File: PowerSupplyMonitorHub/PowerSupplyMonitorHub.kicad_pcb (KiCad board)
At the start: 2 copper layers, 88 parts, among them J1 Input, J10 RJ45 PWR 4, J2 OLED I2C, J3 CON_PCA, J4 RJ45 PWR 0, J5 CON_PCF, J6 RJ45 PWR 1, J7 RJ45 PWR 2, J8 CON_TCA, J9 RJ45 PWR 3, SW1 DIP_PCA, SW2 DIP_PCF, SW3 DIP_TCA, U1 PCA9685PW, U10 PC817, U11 PC817, U12 PC817, U13 PC817, U3 PC817, U4 PC817, U5 PC817, U6 PC817, U7 PC817, U8 PC817, U9 TCA9548APWR

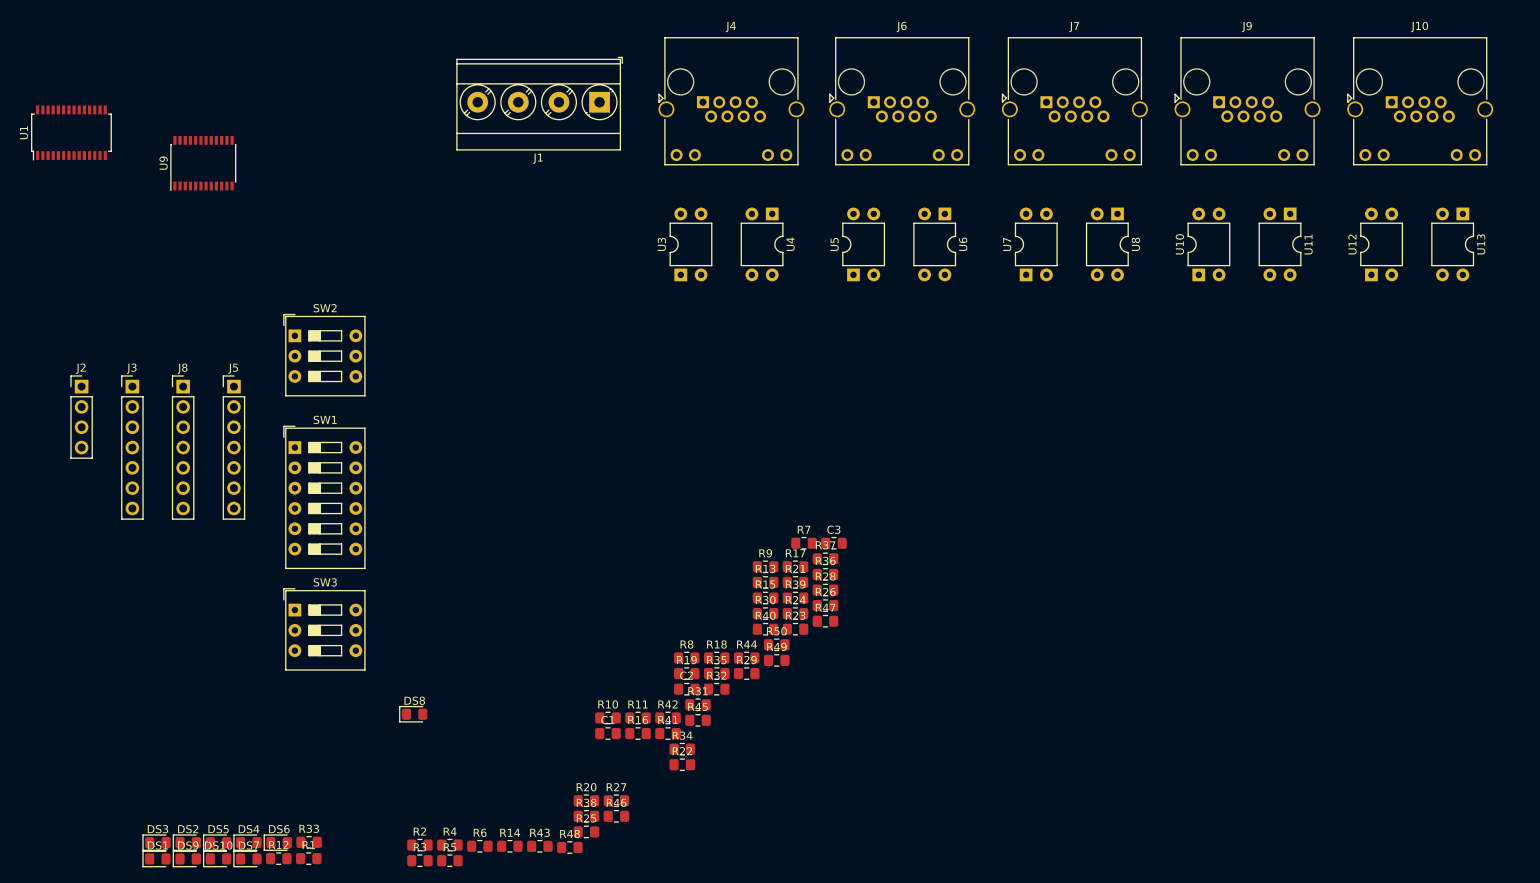
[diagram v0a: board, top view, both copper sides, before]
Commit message: added dip switches to i2c ics for adress selection added pullup resistors to i2c input lines added placeholder footprint for pcf8575 added minimal pcb placement for testing
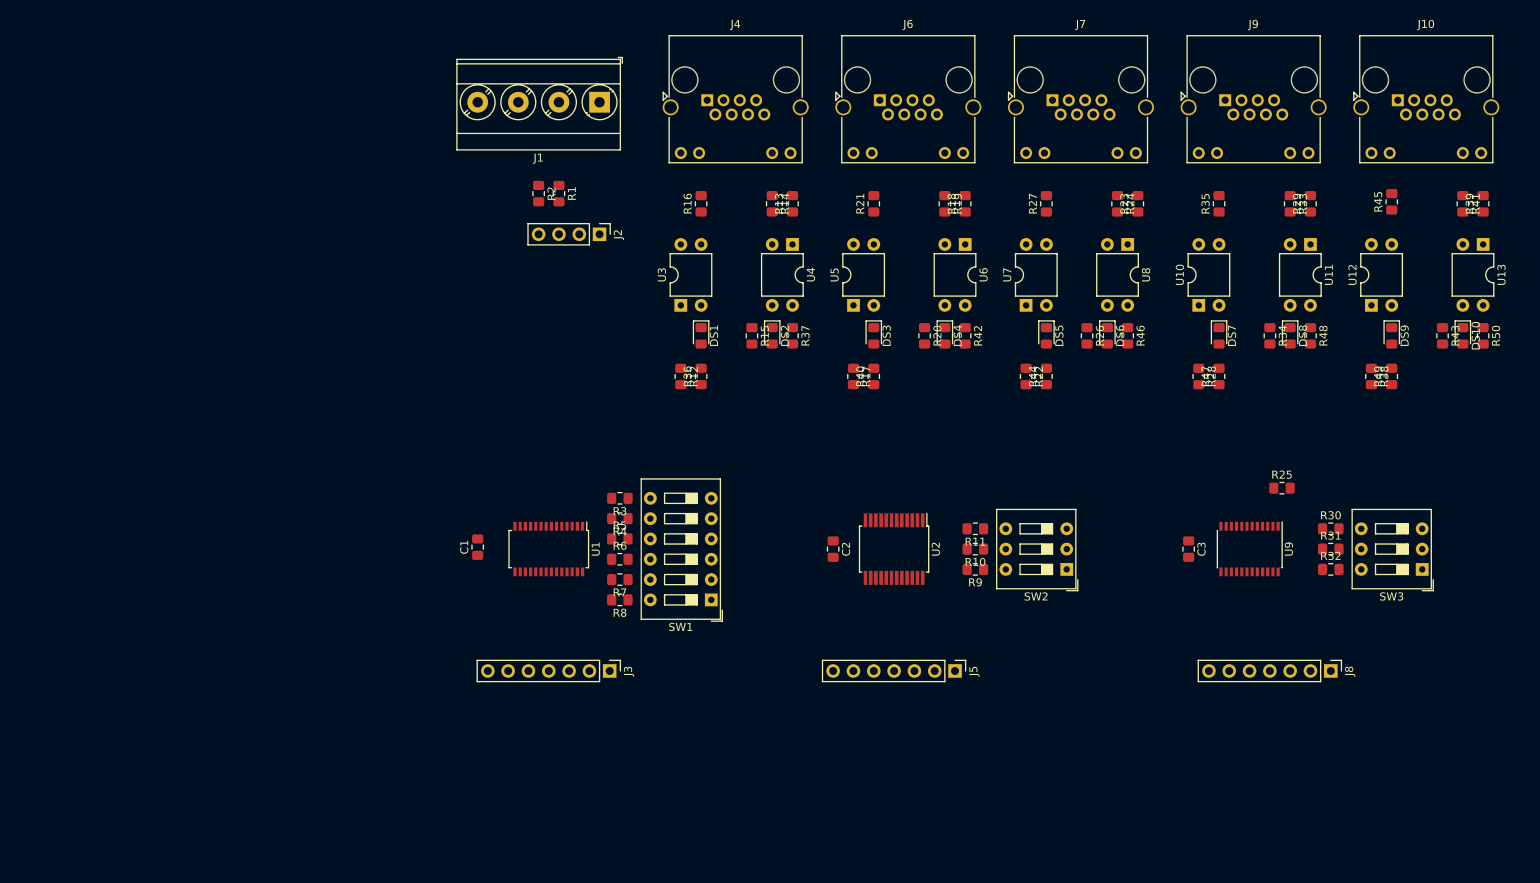
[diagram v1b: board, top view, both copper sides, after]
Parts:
- added U2: PCF8575, Package_SO:SSOP-24_5.3x8.2mm_P0.65mm, F.Cu at (148.6, 94.0)
- DS1: value DC0 -> RC0
- DS10: value RC4 -> DC4
- DS2: value RC0 -> DC0
- DS3: value DC1 -> RC1
- DS4: value RC1 -> DC1
- DS5: value DC2 -> RC2
- DS6: value RC2 -> DC2
- DS7: value DC3 -> RC3
- DS8: value RC3 -> DC3
- DS9: value DC4 -> RC4
- moved DS10 168.8 mm to (219.7, 67.3), turned to 270 degrees
- moved DS9 164.1 mm to (210.8, 67.3), turned to 270 degrees
- moved J8 147.9 mm to (203.2, 109.2), turned to 270 degrees
- moved R33 146.4 mm to (198.1, 50.8), turned to 270 degrees
- moved SW3 141.1 mm to (214.6, 96.5), turned to 180 degrees
- moved U9 139.4 mm to (193.0, 94.0), turned to 270 degrees
- moved DS7 137.8 mm to (189.2, 67.3), turned to 270 degrees
- moved R43 129.7 mm to (217.2, 67.3), turned to 270 degrees
- moved DS6 121.4 mm to (175.3, 67.3), turned to 270 degrees
- moved DS5 121.4 mm to (167.6, 67.3), turned to 270 degrees
- moved R41 119.4 mm to (219.7, 50.8), turned to 270 degrees
- moved DS8 119.3 mm to (198.1, 67.3), turned to 270 degrees
- moved R48 112.6 mm to (200.7, 67.3), turned to 270 degrees
- moved R38 112.5 mm to (208.3, 72.4), turned to 270 degrees
- moved DS3 109.7 mm to (146.1, 67.3), turned to 270 degrees
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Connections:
- DS1 pad 1: /DC_0 -> /RC_0
- DS10 pad 1: /RC_4 -> /DC_4
- DS2 pad 1: /RC_0 -> /DC_0
- DS3 pad 1: /DC_1 -> /RC_1
- DS4 pad 1: /RC_1 -> /DC_1
- DS5 pad 1: /DC_2 -> /RC_2
- DS6 pad 1: /RC_2 -> /DC_2
- DS7 pad 1: /DC_3 -> /RC_3
- DS8 pad 1: /RC_3 -> /DC_3
- DS9 pad 1: /DC_4 -> /RC_4

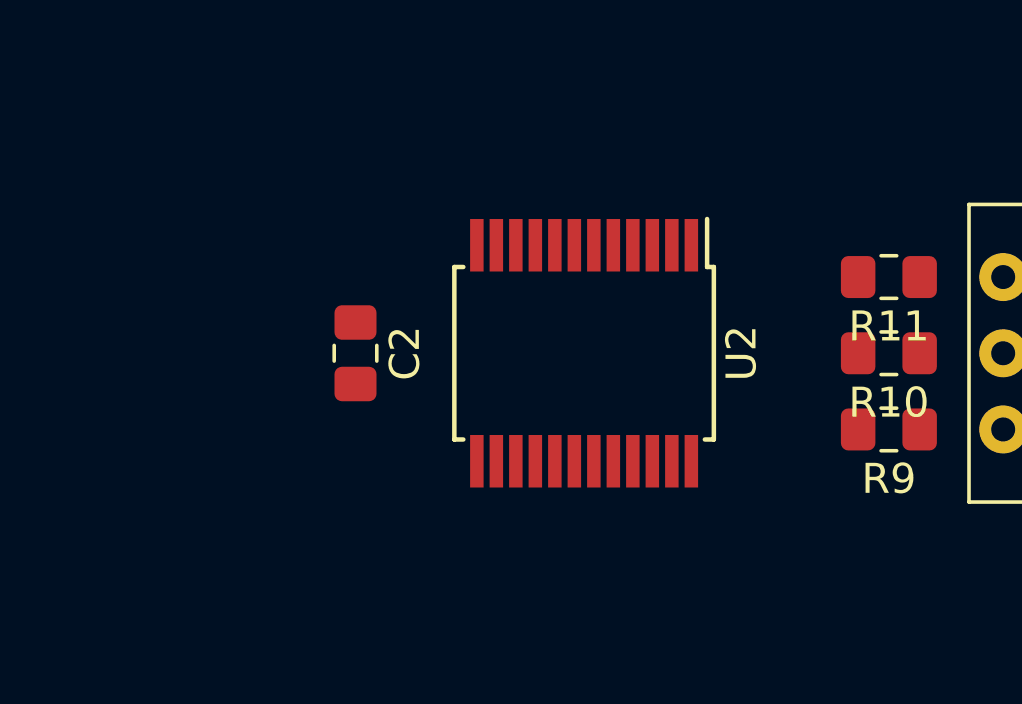
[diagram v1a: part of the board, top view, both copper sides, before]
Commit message: changed package and footprint from sop to soi for pcf8575
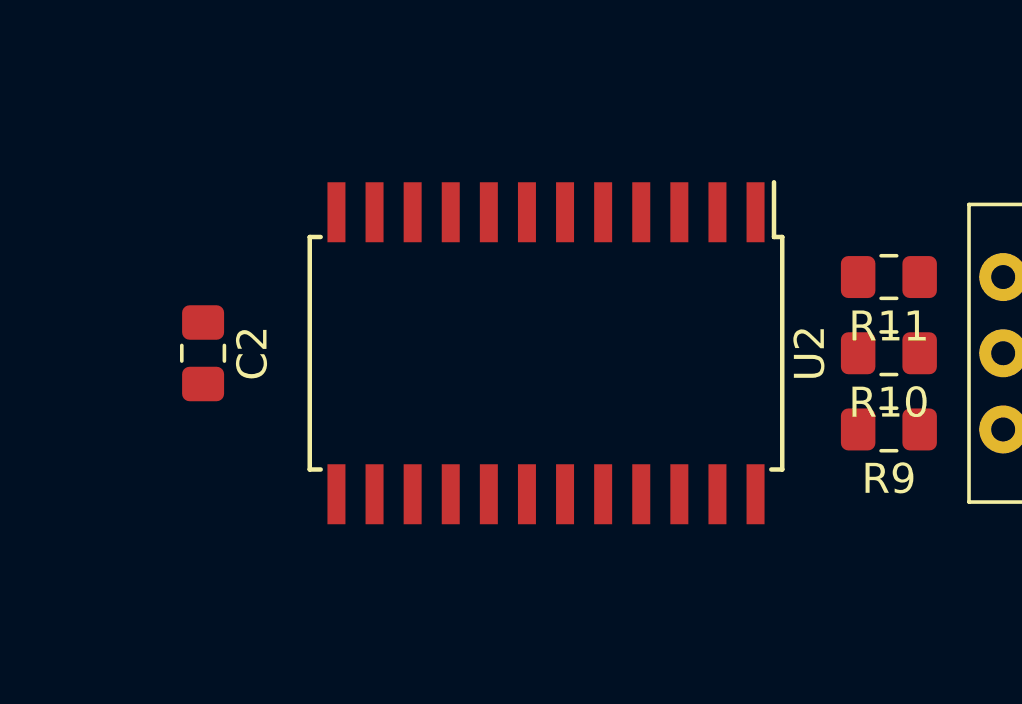
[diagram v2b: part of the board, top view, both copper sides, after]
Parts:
- U2: footprint Package_SO:SSOP-24_5.3x8.2mm_P0.65mm -> Package_SO:SOIC-24W_7.5x15.4mm_P1.27mm
- moved C2 5.08 mm to (135.9, 94.0)
- moved U2 1.27 mm to (147.3, 94.0)

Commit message: added new 3d render of front and back view of pcb added pcb routing from autorouter added power led indicator added i2c ic adress ranges to silkscreen added unused ic pins pinout info silkscreen added power input info silkscreen
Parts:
- added DS11: PWR, LED_SMD:LED_0805_2012Metric_Pad1.15x1.40mm_HandSolder, F.Cu at (104.8, 94.6)
- added G***: LOGO, w_logo:Logo_silk_OSHW_6x6mm, F.Cu at (87.6, 112.4)
- added G***: LOGO, w_logo:Logo_copper_OSHW_6x6mm, B.Cu at (87.6, 112.4)
- added MH1: MountingHole, MountingHole:MountingHole_3.5mm, F.Cu at (86.3, 70.2)
- added MH2: MountingHole, MountingHole:MountingHole_3.5mm, F.Cu at (223.3, 70.2)
- added MH3: MountingHole, MountingHole:MountingHole_3.5mm, F.Cu at (223.3, 124.2)
- added MH4: MountingHole, MountingHole:MountingHole_3.5mm, F.Cu at (86.3, 124.2)
- added R51: 220, Resistor_SMD:R_0805_2012Metric_Pad1.15x1.40mm_HandSolder, F.Cu at (102.2, 94.6)
- J1: value Input -> PCA; footprint TerminalBlock_Phoenix:TerminalBlock_Phoenix_MKDS-3-4-5.08_1x04_P5.08mm_Horizontal -> Connector_PinHeader_2.54mm:PinHeader_1x07_P2.54mm_Vertical
- J10: value RJ45 PWR 4 -> Input; footprint Connector_RJ:RJ45_Amphenol_RJHSE538X -> TerminalBlock_Phoenix:TerminalBlock_Phoenix_MKDS-3-4-5.08_1x04_P5.08mm_Horizontal
- J2: value OLED I2C -> RJ45 PWR 0; footprint Connector_PinHeader_2.54mm:PinHeader_1x04_P2.54mm_Vertical -> Connector_RJ:RJ45_Amphenol_RJHSE538X
- J3: value CON_PCA -> RJ45 PWR 1; footprint Connector_PinHeader_2.54mm:PinHeader_1x07_P2.54mm_Vertical -> Connector_RJ:RJ45_Amphenol_RJHSE538X
- J4: value RJ45 PWR 0 -> RJ45 PWR 2
- J5: value CON_PCF -> RJ45 PWR 3; footprint Connector_PinHeader_2.54mm:PinHeader_1x07_P2.54mm_Vertical -> Connector_RJ:RJ45_Amphenol_RJHSE538X
- J6: value RJ45 PWR 1 -> RJ45 PWR 4
- J7: value RJ45 PWR 2 -> OLED I2C; footprint Connector_RJ:RJ45_Amphenol_RJHSE538X -> Connector_PinHeader_2.54mm:PinHeader_1x04_P2.54mm_Vertical
- J8: value CON_TCA -> TCA
- J9: value RJ45 PWR 3 -> PCF; footprint Connector_RJ:RJ45_Amphenol_RJHSE538X -> Connector_PinHeader_2.54mm:PinHeader_1x07_P2.54mm_Vertical
- R1, R10, R11, R2, R25, R3, R30, R4, R5, R6, R7, R8, R9: value 10K -> 220
- R16, R17, R18, R19, R20, R33, R34, R35, R36, R37, R48, R49, R50: value 220 -> 10K
- SW2: value DIP_PCF -> DIP_TCA
- SW3: value DIP_TCA -> DIP_PCF
- U12: value PC817 -> TCA9548APWR; footprint Package_DIP:DIP-4_W7.62mm -> Package_SO:TSSOP-24_4.4x7.8mm_P0.65mm
- U13: value PC817 -> PCF8575; footprint Package_DIP:DIP-4_W7.62mm -> Package_SO:SOIC-24W_7.5x15.4mm_P1.27mm
- U2: value PCF8575 -> PC817; footprint Package_SO:SOIC-24W_7.5x15.4mm_P1.27mm -> Package_DIP:DIP-4_W7.62mm
- U9: value TCA9548APWR -> PC817; footprint Package_SO:TSSOP-24_4.4x7.8mm_P0.65mm -> Package_DIP:DIP-4_W7.62mm
- moved R33 110.0 mm to (97.2, 94.6), turned to 90 degrees
- moved J10 108.8 mm to (108.6, 73.0), turned to 180 degrees
- moved R39 107.5 mm to (128.9, 104.1), turned to 180 degrees
- moved R32 103.5 mm to (99.7, 94.6), turned to 90 degrees
- moved R36 97.9 mm to (208.9, 121.9)
- moved R38 96.2 mm to (117.5, 104.1), turned to 0 degrees
- moved R37 93.2 mm to (211.5, 121.9), turned to 90 degrees
- moved U13 92.5 mm to (150.5, 114.3)
- moved J9 92.3 mm to (158.1, 124.5), turned to 270 degrees
- moved R41 87.4 mm to (150.5, 104.1), turned to 180 degrees
- moved R15 86.6 mm to (215.3, 86.4), turned to 0 degrees
- moved J1 86.4 mm to (108.6, 124.5), turned to 270 degrees
- moved J7 82.0 mm to (104.8, 89.5), turned to 270 degrees
- moved R31 81.8 mm to (126.4, 121.9), turned to 270 degrees
- moved R18 81.0 mm to (118.7, 121.9), turned to 270 degrees
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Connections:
- DS10 pad 1: /DC_4 -> GND
- DS2 pad 1: /DC_0 -> GND
- DS4 pad 1: /DC_1 -> GND
- DS6 pad 1: /DC_2 -> GND
- DS8 pad 1: /DC_3 -> GND
- J1 pad 2: +5V -> Net-(J1-Pad2)
- J1 pad 3: /SCL -> Net-(J1-Pad3)
- J1 pad 4: /SDA -> Net-(J1-Pad4)
- J10 pad 1: /RC+_4 -> GND
- J10 pad 2: /RC-_4 -> +5V
- J10 pad 3: /DC-OK_4 -> /SCL
- J10 pad 4: /SCL4 -> /SDA
- J2 pad 1: GND -> /RC+_0
- J2 pad 2: +5V -> /RC-_0
- J2 pad 3: /SCL -> /DC-OK_0
- J2 pad 4: /SDA -> /SCL0
- J3 pad 1: GND -> /RC+_1
- J3 pad 2: Net-(J3-Pad2) -> /RC-_1
- J3 pad 3: Net-(J3-Pad3) -> /DC-OK_1
- J3 pad 4: Net-(J3-Pad4) -> /SCL1
- J3 pad 5: Net-(J3-Pad5) -> GND
- J3 pad 6: Net-(J3-Pad6) -> /DC-GND_1
- J3 pad 7: Net-(J3-Pad7) -> /SDA1
- J4 pad 1: /RC+_0 -> /RC+_2
- J4 pad 2: /RC-_0 -> /RC-_2
- J4 pad 3: /DC-OK_0 -> /DC-OK_2
- J4 pad 4: /SCL0 -> /SCL2
- J4 pad 6: /DC-GND_0 -> /DC-GND_2
- J4 pad 7: /SDA0 -> /SDA2
- J5 pad 1: +5V -> /RC+_3
- J5 pad 2: Net-(J5-Pad2) -> /RC-_3
- J5 pad 3: Net-(J5-Pad3) -> /DC-OK_3
- J5 pad 4: Net-(J5-Pad4) -> /SCL3
- J5 pad 5: Net-(J5-Pad5) -> GND
- J5 pad 6: Net-(J5-Pad6) -> /DC-GND_3
- J5 pad 7: Net-(J5-Pad7) -> /SDA3
- J6 pad 1: /RC+_1 -> /RC+_4
- J6 pad 2: /RC-_1 -> /RC-_4
- J6 pad 3: /DC-OK_1 -> /DC-OK_4
- J6 pad 4: /SCL1 -> /SCL4
- J6 pad 6: /DC-GND_1 -> /DC-GND_4
- J6 pad 7: /SDA1 -> /SDA4
- J7 pad 1: /RC+_2 -> GND
- J7 pad 2: /RC-_2 -> +5V
- J7 pad 3: /DC-OK_2 -> /SCL
- J7 pad 4: /SCL2 -> /SDA
- J9 pad 1: /RC+_3 -> +5V
- J9 pad 2: /RC-_3 -> Net-(J9-Pad2)
- J9 pad 3: /DC-OK_3 -> Net-(J9-Pad3)
- J9 pad 4: /SCL3 -> Net-(J9-Pad4)
- J9 pad 5: GND -> Net-(J9-Pad5)
- J9 pad 6: /DC-GND_3 -> Net-(J9-Pad6)
- J9 pad 7: /SDA3 -> Net-(J9-Pad7)
- R1 pad 1: +5V -> /DATA_0
- R1 pad 2: /SCL -> Net-(J2-Pad12)
- R10 pad 1: Net-(R10-Pad1) -> /LINK_4
- R10 pad 2: GND -> Net-(J6-Pad10)
- R11 pad 1: Net-(R11-Pad1) -> /DC-OK_0
- R11 pad 2: GND -> Net-(R11-Pad2)
- R12 pad 1: Net-(R12-Pad1) -> /DC-OK_1
- R12 pad 2: +5V -> Net-(R12-Pad2)
- R13 pad 1: /DATA_0 -> /DC-OK_2
- R13 pad 2: Net-(J4-Pad12) -> Net-(R13-Pad2)
- R14 pad 1: /DC-OK_0 -> /DC-OK_3
- R15 pad 1: /DC_0 -> /DC-OK_4
- R15 pad 2: GND -> Net-(R15-Pad2)
- R16 pad 1: /LINK_0 -> Net-(R16-Pad1)
- R16 pad 2: Net-(J4-Pad10) -> GND
- R17 pad 2: +5V -> GND
- R18 pad 1: /DATA_1 -> Net-(R18-Pad1)
- R18 pad 2: Net-(J6-Pad12) -> GND
- R19 pad 1: /DC-OK_1 -> Net-(R19-Pad1)
- R19 pad 2: Net-(R19-Pad2) -> GND
- R2 pad 1: +5V -> /LINK_0
- R2 pad 2: /SDA -> Net-(J2-Pad10)
- R20 pad 1: /DC_1 -> Net-(R20-Pad1)
- R21 pad 1: /LINK_1 -> Net-(R21-Pad1)
- R21 pad 2: Net-(J6-Pad10) -> +5V
- R23 pad 1: /DATA_2 -> Net-(R23-Pad1)
- R23 pad 2: Net-(J7-Pad12) -> +5V
- R24 pad 1: /DC-OK_2 -> Net-(R24-Pad1)
- R24 pad 2: Net-(R24-Pad2) -> +5V
- R26 pad 1: /DC_2 -> Net-(R26-Pad1)
- R26 pad 2: GND -> +5V
- R27 pad 1: /LINK_2 -> Net-(R27-Pad1)
- R27 pad 2: Net-(J7-Pad10) -> +5V
- R29 pad 1: /DATA_3 -> Net-(R29-Pad1)
- R29 pad 2: Net-(J9-Pad12) -> +5V
- R3 pad 1: Net-(R3-Pad1) -> /DATA_1
- R3 pad 2: GND -> Net-(J3-Pad12)
- R30 pad 1: GND -> Net-(R30-Pad1)
- R30 pad 2: Net-(R30-Pad2) -> +5V
- R31 pad 1: GND -> Net-(R31-Pad1)
- R31 pad 2: Net-(R31-Pad2) -> GND
- R32 pad 1: GND -> +5V
- R32 pad 2: Net-(R32-Pad2) -> /SCL
- R33 pad 1: /DC-OK_3 -> +5V
- R33 pad 2: Net-(R33-Pad2) -> /SDA
- R34 pad 1: /DC_3 -> GND
- R34 pad 2: GND -> Net-(R34-Pad2)
- R35 pad 1: /LINK_3 -> Net-(R35-Pad1)
- R35 pad 2: Net-(J9-Pad10) -> +5V
- R36 pad 1: +5V -> GND
- R36 pad 2: Net-(DS1-Pad2) -> Net-(R36-Pad2)
- R37 pad 1: +5V -> GND
- R37 pad 2: Net-(DS2-Pad2) -> Net-(R37-Pad2)
- R38 pad 1: Net-(R38-Pad1) -> +5V
- R38 pad 2: +5V -> Net-(DS1-Pad2)
- R39 pad 1: /DATA_4 -> +5V
- R39 pad 2: Net-(J10-Pad12) -> Net-(DS2-Pad2)
- R4 pad 1: Net-(R4-Pad1) -> /LINK_1
- R4 pad 2: GND -> Net-(J3-Pad10)
- R41 pad 1: /DC-OK_4 -> +5V
- R41 pad 2: Net-(R41-Pad2) -> Net-(DS4-Pad2)
- R42 pad 2: Net-(DS4-Pad2) -> Net-(DS5-Pad2)
- R43 pad 1: /DC_4 -> +5V
- R43 pad 2: GND -> Net-(DS6-Pad2)
- R44 pad 2: Net-(DS5-Pad2) -> Net-(DS7-Pad2)
- R45 pad 1: /LINK_4 -> +5V
- R45 pad 2: Net-(J10-Pad10) -> Net-(DS8-Pad2)
- R46 pad 2: Net-(DS6-Pad2) -> Net-(DS9-Pad2)
- R47 pad 2: Net-(DS7-Pad2) -> Net-(DS10-Pad2)
- R48 pad 1: +5V -> Net-(R48-Pad1)
- R48 pad 2: Net-(DS8-Pad2) -> GND
- R49 pad 1: +5V -> Net-(R49-Pad1)
- R49 pad 2: Net-(DS9-Pad2) -> GND
- R5 pad 1: Net-(R5-Pad1) -> /DATA_2
- R5 pad 2: GND -> Net-(J4-Pad12)
- R50 pad 1: +5V -> Net-(R50-Pad1)
- R50 pad 2: Net-(DS10-Pad2) -> GND
- R6 pad 1: Net-(R6-Pad1) -> /LINK_2
- R6 pad 2: GND -> Net-(J4-Pad10)
- R7 pad 1: Net-(R7-Pad1) -> /DATA_3
- R7 pad 2: GND -> Net-(J5-Pad12)
- R8 pad 1: Net-(R8-Pad1) -> /LINK_3
- R8 pad 2: GND -> Net-(J5-Pad10)
- R9 pad 1: Net-(R9-Pad1) -> /DATA_4
- R9 pad 2: GND -> Net-(J6-Pad12)
- SW1 pad 10: Net-(R6-Pad1) -> Net-(R19-Pad1)
- SW1 pad 11: Net-(R7-Pad1) -> Net-(R20-Pad1)
- SW1 pad 12: Net-(R8-Pad1) -> Net-(R31-Pad1)
- SW1 pad 7: Net-(R3-Pad1) -> Net-(R16-Pad1)
- SW1 pad 8: Net-(R4-Pad1) -> Net-(R17-Pad1)
- SW1 pad 9: Net-(R5-Pad1) -> Net-(R18-Pad1)
- SW2 pad 4: Net-(R11-Pad1) -> Net-(R34-Pad2)
- SW2 pad 5: Net-(R10-Pad1) -> Net-(R36-Pad2)
- SW2 pad 6: Net-(R9-Pad1) -> Net-(R37-Pad2)
- SW3 pad 4: Net-(R30-Pad2) -> Net-(R50-Pad1)
- SW3 pad 5: Net-(R31-Pad2) -> Net-(R49-Pad1)
- SW3 pad 6: Net-(R32-Pad2) -> Net-(R48-Pad1)
- U1 pad 1: Net-(R8-Pad1) -> Net-(R31-Pad1)
- U1 pad 17: Net-(J3-Pad7) -> Net-(J1-Pad7)
- U1 pad 18: Net-(J3-Pad6) -> Net-(J1-Pad6)
- U1 pad 19: Net-(J3-Pad5) -> Net-(J1-Pad5)
- U1 pad 2: Net-(R7-Pad1) -> Net-(R20-Pad1)
- U1 pad 20: Net-(J3-Pad4) -> Net-(J1-Pad4)
- U1 pad 21: Net-(J3-Pad3) -> Net-(J1-Pad3)
- U1 pad 22: Net-(J3-Pad2) -> Net-(J1-Pad2)
- U1 pad 24: Net-(R3-Pad1) -> Net-(R16-Pad1)
- U1 pad 3: Net-(R6-Pad1) -> Net-(R19-Pad1)
- U1 pad 4: Net-(R5-Pad1) -> Net-(R18-Pad1)
- U1 pad 5: Net-(R4-Pad1) -> Net-(R17-Pad1)
- U10 pad 1: Net-(R28-Pad1) -> Net-(R29-Pad1)
- U10 pad 2: /RC_3 -> /RC_4
- U10 pad 3: /RC-_3 -> /RC-_4
- U10 pad 4: /RC+_3 -> /RC+_4
- U11 pad 1: Net-(R33-Pad2) -> Net-(R15-Pad2)
- U11 pad 2: /DC-GND_3 -> /DC-GND_4
- U11 pad 3: /DC_3 -> GND
- U11 pad 4: +5V -> Net-(R30-Pad1)
- U12 pad 1: Net-(R38-Pad1) -> Net-(R34-Pad2)
- U12 pad 2: /RC_4 -> Net-(R36-Pad2)
- U12 pad 3: /RC-_4 -> Net-(R35-Pad1)
- U12 pad 4: /RC+_4 -> /SDA0
- U13 pad 1: Net-(R41-Pad2) -> Net-(U13-Pad1)
- U13 pad 2: /DC-GND_4 -> Net-(R49-Pad1)
- U13 pad 3: /DC_4 -> Net-(R50-Pad1)
- U13 pad 4: +5V -> /RC_0
- U2 pad 1: Net-(U2-Pad1) -> Net-(R21-Pad1)
- U2 pad 2: Net-(R10-Pad1) -> /RC_0
- U2 pad 3: Net-(R11-Pad1) -> /RC-_0
- U2 pad 4: /RC_0 -> /RC+_0
- U3 pad 1: Net-(R12-Pad1) -> Net-(R11-Pad2)
- U3 pad 2: /RC_0 -> /DC-GND_0
- U3 pad 3: /RC-_0 -> GND
- U3 pad 4: /RC+_0 -> Net-(R22-Pad1)
- U4 pad 1: Net-(R14-Pad2) -> Net-(R23-Pad1)
- U4 pad 2: /DC-GND_0 -> /RC_1
- U4 pad 3: /DC_0 -> /RC-_1
- U4 pad 4: +5V -> /RC+_1
- U5 pad 1: Net-(R17-Pad1) -> Net-(R12-Pad2)
- U5 pad 2: /RC_1 -> /DC-GND_1
- U5 pad 3: /RC-_1 -> GND
- U5 pad 4: /RC+_1 -> Net-(R24-Pad1)
- U6 pad 1: Net-(R19-Pad2) -> Net-(R25-Pad1)
- U6 pad 2: /DC-GND_1 -> /RC_2
- U6 pad 3: /DC_1 -> /RC-_2
- U6 pad 4: +5V -> /RC+_2
- U7 pad 1: Net-(R22-Pad1) -> Net-(R13-Pad2)
- U7 pad 2: /RC_2 -> /DC-GND_2
- U7 pad 3: /RC-_2 -> GND
- U7 pad 4: /RC+_2 -> Net-(R26-Pad1)
- U8 pad 1: Net-(R24-Pad2) -> Net-(R27-Pad1)
- U8 pad 2: /DC-GND_2 -> /RC_3
- U8 pad 3: /DC_2 -> /RC-_3
- U8 pad 4: +5V -> /RC+_3
- U9 pad 1: Net-(R30-Pad2) -> Net-(R14-Pad2)
- U9 pad 2: Net-(R31-Pad2) -> /DC-GND_3
- U9 pad 3: Net-(R25-Pad1) -> GND
- U9 pad 4: /SDA0 -> Net-(R28-Pad1)
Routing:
- net +5V: track 0.00 -> 467.5 mm, vias 0 -> 2
- net /SDA: track 0.00 -> 176.6 mm
- net /DATA_4: track 0.00 -> 175.7 mm
- net /LINK_4: track 0.00 -> 156.8 mm
- net /SCL: track 0.00 -> 156.3 mm, vias 0 -> 3
- net /DATA_3: track 0.00 -> 109.3 mm
- net /LINK_3: track 0.00 -> 99.3 mm
- net /SCL0: track 0.00 -> 94.5 mm, vias 0 -> 1
- net /SDA0: track 0.00 -> 91.2 mm, vias 0 -> 1
- net /DATA_2: track 0.00 -> 83.7 mm
- net /LINK_2: track 0.00 -> 79.4 mm
- net /RC_4: track 0.00 -> 76.3 mm
- net /SCL1: track 0.00 -> 71.6 mm, vias 0 -> 1
- net /LINK_1: track 0.00 -> 69.4 mm
- net /DATA_1: track 0.00 -> 68.8 mm, vias 0 -> 2
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- added copper zone on B.Cu, net GND
- added copper zone on F.Cu, net GND
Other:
- board outline added: 145 x 62 mm
- board text added: "0x40 - 0x4E"
- board text added: "0x40 - 0x80"
- board text added: "0x70 - 0x77"
- board text added: "10,11,12,13,14,15,GND"
- board text added: "12,13,14,15,16,17,+5V"
- board text added: "C5,D5,C6,D6,C7,D7,+5V"
- board text added: "Elektrospy HRPG I²C Hub ver.1.0"
- board text added: "I²C OLED"
- board text added: "PWR"
- board text added: "SDA SCL +5V GND"
